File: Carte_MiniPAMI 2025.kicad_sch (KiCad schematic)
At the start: 63 parts, among them J1 ${MANUFACTURER PART NUMBER}, J11 ${MANUFACTURER PART NUMBER}, J2 ${MANUFACTURER PART NUMBER}, J8 ${MANUFACTURER PART NUMBER}, J9 ${MANUFACTURER PART NUMBER}, J91 ${MANUFACTURER PART NUMBER}, J92 ${MANUFACTURER PART NUMBER}, J93 ${MANUFACTURER PART NUMBER}, J98 ${MANUFACTURER PART NUMBER}, J99 ${MANUFACTURER PART NUMBER}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

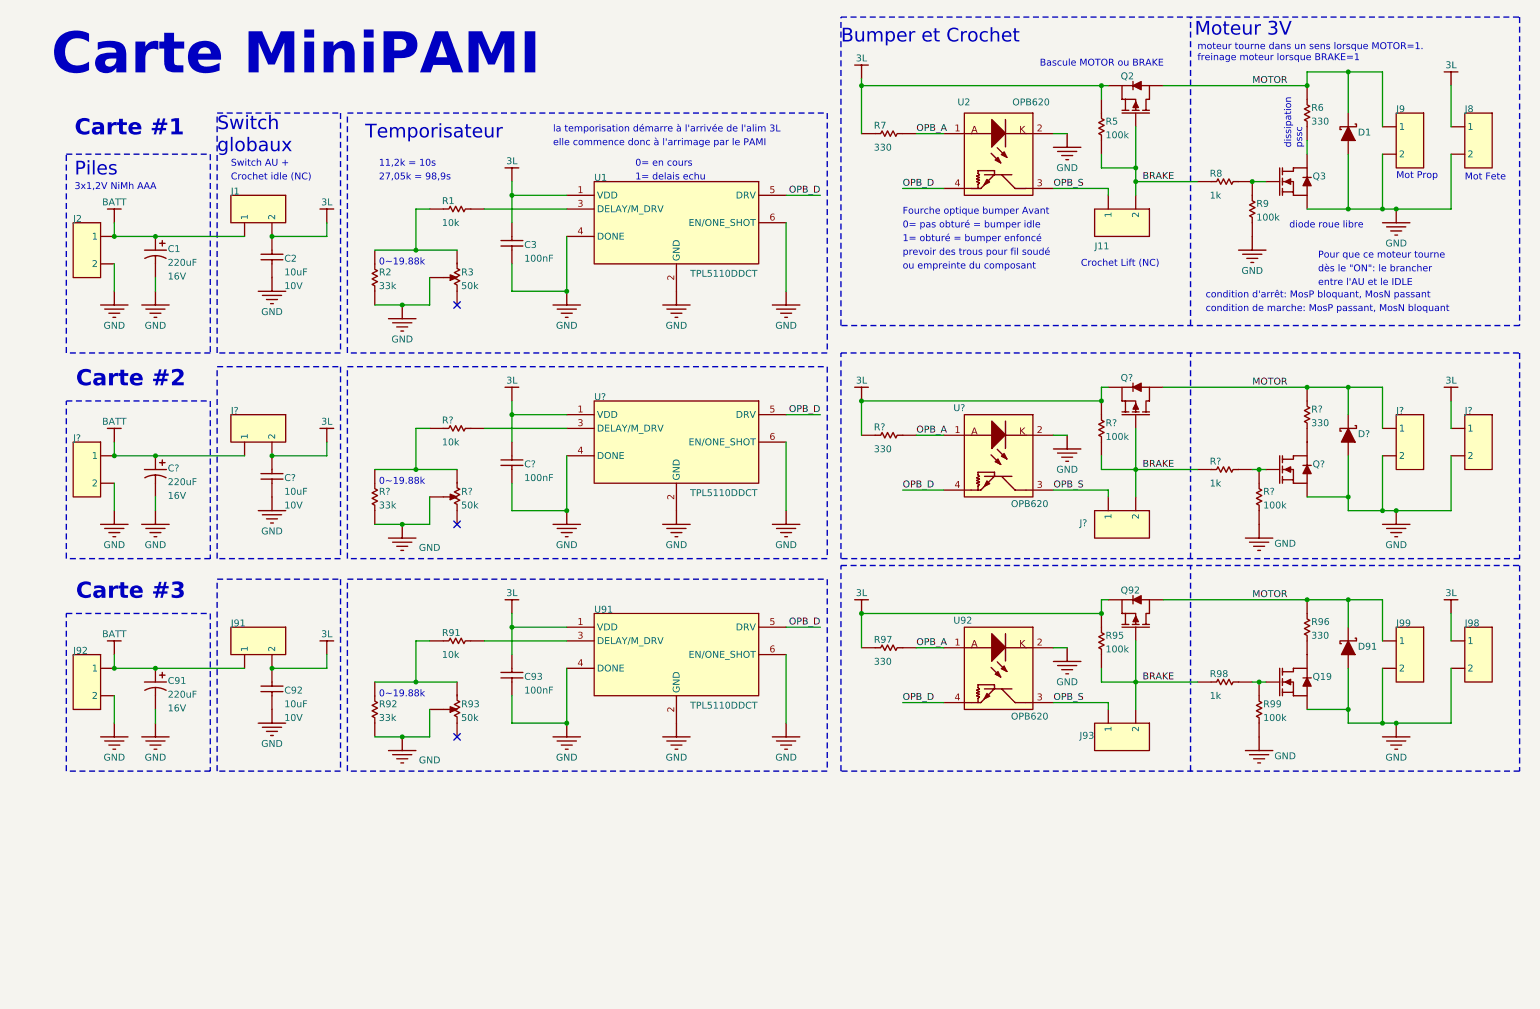
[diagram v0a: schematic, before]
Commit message: corrrection footprint trim, ajout R64, config JLCPCB ASSY, fin panelisation (TODO: revue et cmd)
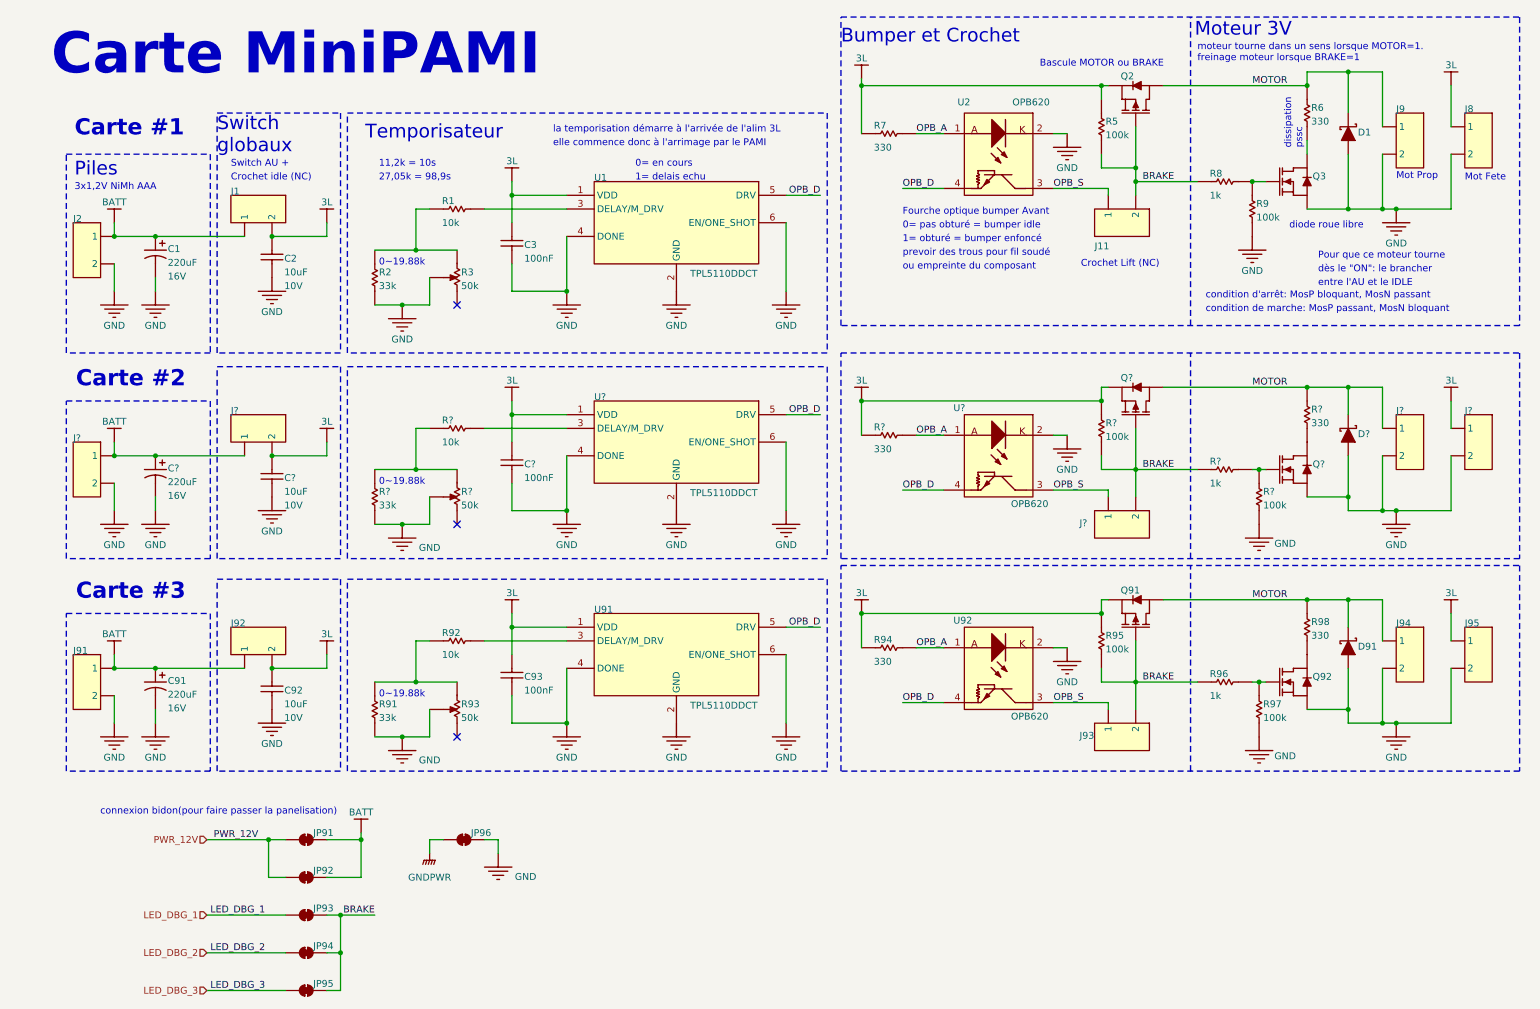
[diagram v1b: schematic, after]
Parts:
- added JP91, JP92, JP93, JP94, JP95, JP96: SolderJumper_2_Bridged, 12V-actuators_pcb:R_0402_1005Metric_jumperClosed, symbol Jumper:SolderJumper_2_Bridged
- C1, C91, C?: value ${ALTIUM_VALUE} -> 220uF
- C2, C92, C?: value ${ALTIUM_VALUE} -> 10uF; LCSC (none) -> C440198
- C3, C93, C?: value ${ALTIUM_VALUE} -> 100nF; LCSC (none) -> C14663
- D1, D91, D?: value ${MANUFACTURER PART NUMBER} -> RBR3MM40ATFTR; LCSC (none) -> C81598
- J1, J11, J2, J8, J9, J93, J? (x5): value ${MANUFACTURER PART NUMBER} -> 22-03-2021
- J91: renamed from J92; value ${MANUFACTURER PART NUMBER} -> 22-03-2021
- J92: renamed from J91; value ${MANUFACTURER PART NUMBER} -> 22-03-2021
- J94: renamed from J99; value ${MANUFACTURER PART NUMBER} -> 22-03-2021
- J95: renamed from J98; value ${MANUFACTURER PART NUMBER} -> 22-03-2021
- Q2, Q?: value ${MANUFACTURER PART NUMBER} -> ZXM61P03FTA; LCSC (none) -> C15127
- Q3, Q?: value ${MANUFACTURER PART NUMBER} -> IRLML0040TRPBF; LCSC (none) -> C20917
- Q91: renamed from Q92; value ${MANUFACTURER PART NUMBER} -> ZXM61P03FTA; LCSC (none) -> C15127
- Q92: renamed from Q19; value ${MANUFACTURER PART NUMBER} -> IRLML0040TRPBF; LCSC (none) -> C20917
- R1, R?: value ${MANUFACTURER PART NUMBER} -> RC0603FR-0710KL; LCSC (none) -> C25804
- R2, R?: value ${MANUFACTURER PART NUMBER} -> 33k; LCSC (none) -> C4216
- R3, R93, R?: value ${MANUFACTURER PART NUMBER} -> EVM2WSX80B54; footprint TRIM_PANASONIC_EVM-2W -> Potentiometer_SMD:Potentiometer_Bourns_TC33X_Vertical; LCSC (none) -> C913246
- R5, R9, R95, R? (x2): value ${MANUFACTURER PART NUMBER} -> RC0603FR-07100KL; LCSC (none) -> C25803
- R6, R7, R? (x2): value ${MANUFACTURER PART NUMBER} -> RC0603FR-07330RL; LCSC (none) -> C23138
- R8, R?: value ${MANUFACTURER PART NUMBER} -> RC0603FR-071KL; LCSC (none) -> C21190
- R91: renamed from R92; value ${MANUFACTURER PART NUMBER} -> 33k; LCSC (none) -> C4216
- R92: renamed from R91; value ${MANUFACTURER PART NUMBER} -> RC0603FR-0710KL; LCSC (none) -> C25804
- R94: renamed from R97; value ${MANUFACTURER PART NUMBER} -> RC0603FR-07330RL; LCSC (none) -> C23138
- R96: renamed from R98; value ${MANUFACTURER PART NUMBER} -> RC0603FR-071KL; LCSC (none) -> C21190
- R97: renamed from R99; value ${MANUFACTURER PART NUMBER} -> RC0603FR-07100KL; LCSC (none) -> C25803
- R98: renamed from R96; value ${MANUFACTURER PART NUMBER} -> RC0603FR-07330RL; LCSC (none) -> C23138
- U1, U91, U?: value ${MANUFACTURER PART NUMBER} -> TPL5110DDCT; LCSC (none) -> C125830
- U2, U92, U?: value ${MANUFACTURER PART NUMBER} -> OPB620
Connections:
- net BATT: now also JP91.2 (B), JP92.1 (A)
- net BRAKE: now also JP93.1 (A), JP94.1 (A), JP95.1 (A)
- net GND: now also JP96.1 (A)
- new net GNDPWR: JP96.2 (B)
- new net LED_DBG_1: JP93.2 (B)
- new net LED_DBG_2: JP94.2 (B)
- new net LED_DBG_3: JP95.2 (B)
- new net PWR_12V: JP91.1 (A), JP92.2 (B)
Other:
- note added: "connexion bidon(pour faire passer la panelisation)"

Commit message: Maj crystal et connection therminque DC-DC
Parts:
- C1: LCSC (none) -> C440198
- C2: LCSC C440198 -> C1588
- D1: LCSC C81598 -> C191023
- Q2: LCSC C15127 -> C20917
- R3: LCSC C913246 -> C25804
- R5: LCSC C25803 -> C23192
- R6: LCSC C23138 -> C23345
- R7: LCSC C23138 -> C25803
- R9: LCSC C25803 -> C25804
- U1: LCSC C125830 -> C7376
- U2: LCSC (none) -> C182421
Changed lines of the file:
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@@
 			)
 		)
-		(property "LCSC" "C440198"
+		(property "LCSC" "C1588"
 			(at 53.34 53.34 0)
 			(effects
@@
 			)
 		)
-		(property "LCSC" "C23138"
+		(property "LCSC" "C25803"
 			(at 162.56 34.29 0)
 			(effects
@@
 			)
 		)
-		(property "LCSC" "C125830"
+		(property "LCSC" "C7376"
 			(at 113.03 43.18 0)
 			(effects
@@
 			)
 		)
-		(property "LCSC" "C25803"
+		(property "LCSC" "C23192"
 			(at 207.01 38.1 0)
 			(effects
@@
 			)
 		)
+		(property "LCSC" "C440198"
+			(at 34.036 56.388 0)
+			(effects
+				(font
+					(size 1.27 1.27)
+				)
+				(hide yes)
+			)
+		)
 		(pin "1"
 		)
@@
 			)
 		)
+		(property "LCSC" "C182421"
+			(at 180.34 29.21 0)
+			(effects
+				(font
+					(size 1.27 1.27)
+				)
+				(hide yes)
+			)
+		)
 		(pin "1"
 		)
@@
 			)
 		)
-		(property "LCSC" "C913246"
+		(property "LCSC" "C25804"
 			(at 87.63 55.88 0)
 			(effects
@@
 			)
 		)
-		(property "LCSC" "C81598"
+		(property "LCSC" "C191023"
 			(at 252.73 38.1 0)
 			(effects
@@
 			)
 		)
-		(property "LCSC" "C23138"
+		(property "LCSC" "C23345"
 			(at 245.11 35.56 0)
 			(effects
@@
 			)
 		)
-		(property "LCSC" "C25803"
+		(property "LCSC" "C25804"
 			(at 234.95 53.34 0)
 			(effects
@@
 			)
 		)
-		(property "LCSC" "C15127"
+		(property "LCSC" "C20917"
 			(at 213.36 33.02 0)
 			(effects

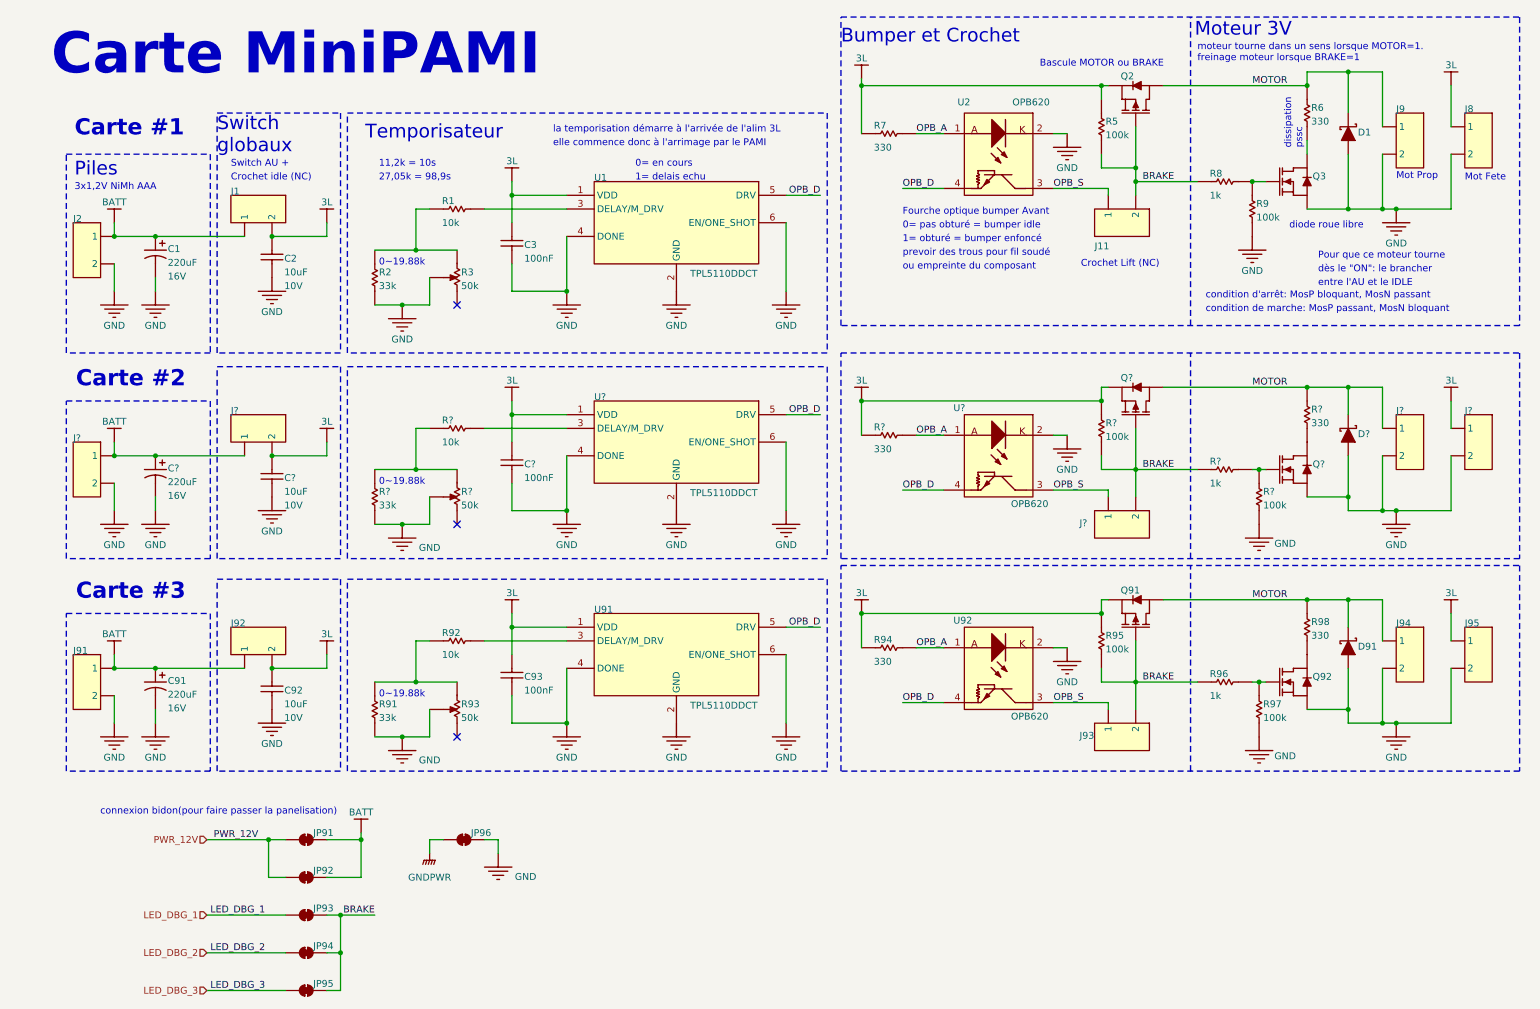
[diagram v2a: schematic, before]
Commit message: PAMI seuls + ajout carte impro
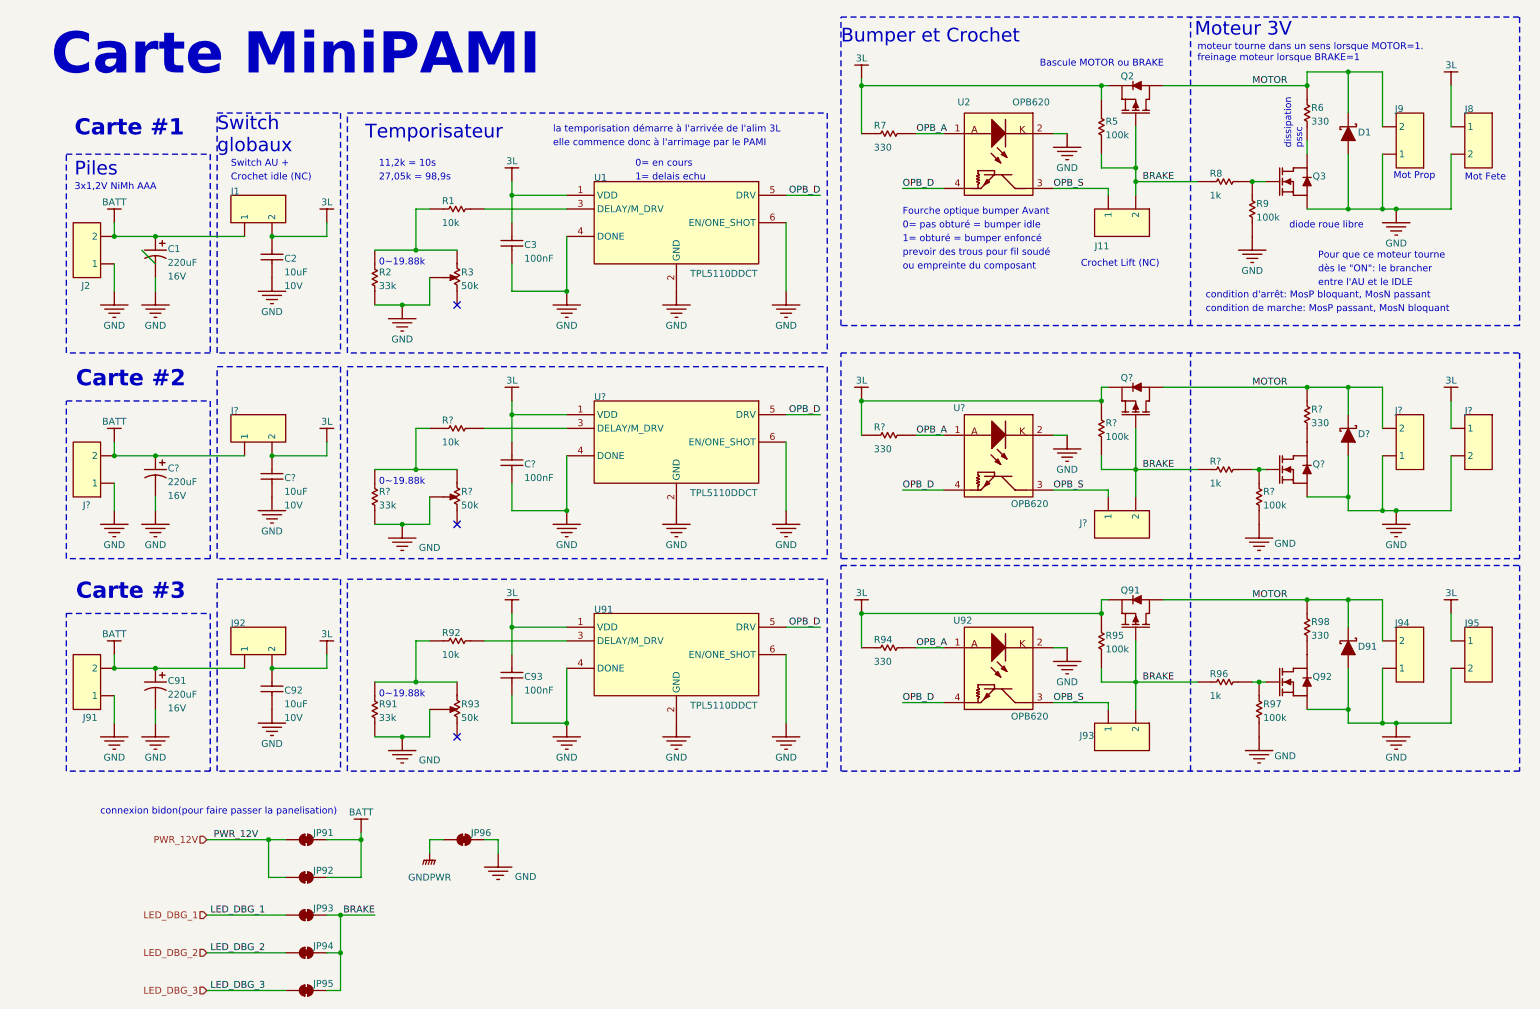
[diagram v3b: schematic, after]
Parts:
- J2, J9, J91, J94, J? (x2): footprint Connector_PinHeader_2.54mm:PinHeader_1x02_P2.54mm_Vertical -> Connector_JST:JST_SH_BM02B-SRSS-TB_1x02-1MP_P1.00mm_Vertical
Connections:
- net BATT: now also J2.2, J91.2, J?.2; no longer J2.1, J91.1, J?.1
- net GND: now also J2.1, J9.1, J91.1, J94.1, J?.1, J?.1; no longer J2.2, J9.2, J91.2, J94.2, J?.2, J?.2
- net MOTOR: now also J9.2, J94.2, J?.2; no longer J9.1, J94.1, J?.1
